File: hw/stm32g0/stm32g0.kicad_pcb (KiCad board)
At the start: 4 copper layers, 80 x 40 mm, 62 parts, among them J101 Barrel_Jack_Switch, J102 Screw_Terminal_01x03, J201 Conn_01x06, J202 Conn_01x04, J203 Conn_01x03, Q101 BC817, SW401 SW_Push, SW402 SW_Push, SW403 SW_Push, SW404 SW_Push, SW405 SW_Push, SW406 SW_Push, U201 STM32G030K8Tx, U202 74AHCT125, U203 CAT24C256, U301 VS1838B, U401 4050, U501 AMS1117-3.3

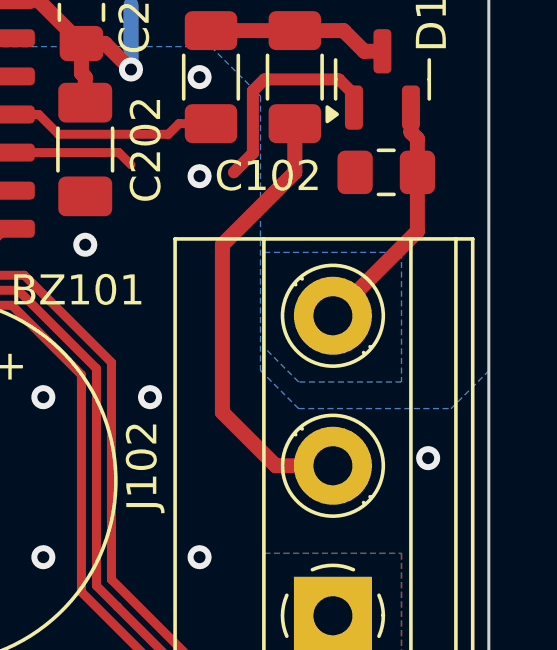
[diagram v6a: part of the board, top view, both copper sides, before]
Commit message: chore(hw): add cable connector identifiers
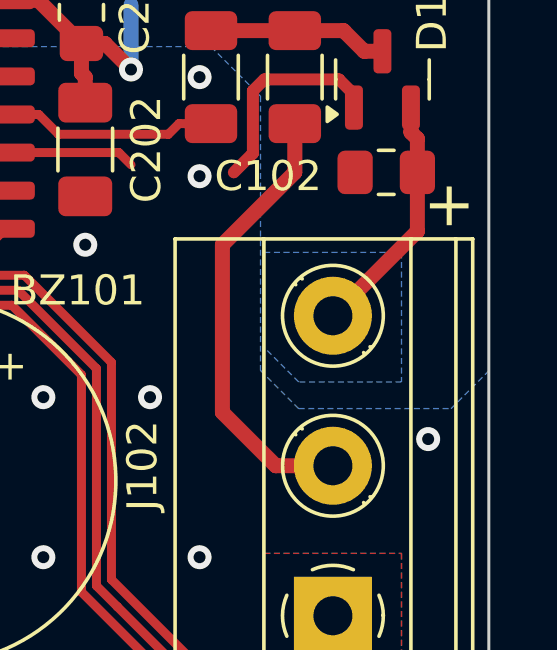
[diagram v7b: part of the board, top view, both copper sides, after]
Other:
- board text added: "+"
- board text added: "-"
- board text added: "D"
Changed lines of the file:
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@@
 		)
 	)
+	(gr_text "D"
+		(at 196.342 93.853 -90)
+		(layer "B.SilkS")
+		(effects
+			(font
+				(size 1.5 1.5)
+				(thickness 0.15)
+			)
+			(justify left bottom)
+		)
+	)
+	(gr_text "-"
+		(at 196.342 98.679 -90)
+		(layer "B.SilkS")
+		(effects
+			(font
+				(size 1.5 1.5)
+				(thickness 0.15)
+			)
+			(justify left bottom)
+		)
+	)
 	(gr_text "JLCJLCJLCJLC"
 		(at 186.563 76.835 0)
@@
 		)
 	)
+	(gr_text "+"
+		(at 196.342 88.646 -90)
+		(layer "B.SilkS")
+		(effects
+			(font
+				(size 1.5 1.5)
+				(thickness 0.15)
+			)
+			(justify left bottom)
+		)
+	)
 	(gr_text "R"
 		(at 174.752 81.788 0)
@@
 		)
 	)
+	(gr_text "+"
+		(at 197.231 85.09 270)
+		(layer "F.SilkS")
+		(effects
+			(font
+				(size 1.5 1.5)
+				(thickness 0.15)
+			)
+			(justify left bottom)
+		)
+	)
 	(gr_text "G"
 		(at 174.752 86.36 0)
@@
 	)
 	(via
-		(at 197.358 94.361)
+		(at 197.358 93.726)
 		(size 0.8)
 		(drill 0.4)
@@
 	)
 	(group ""
+		(members "ac98b90d-8acc-4557-9752-f28e7031f9e1" "acbd161f-f8ce-4742-a507-e40d7ef71db5"
+			"f7fb9be6-987a-44a3-bb12-16e19cd526a0"
+		)
+	)
+	(group ""

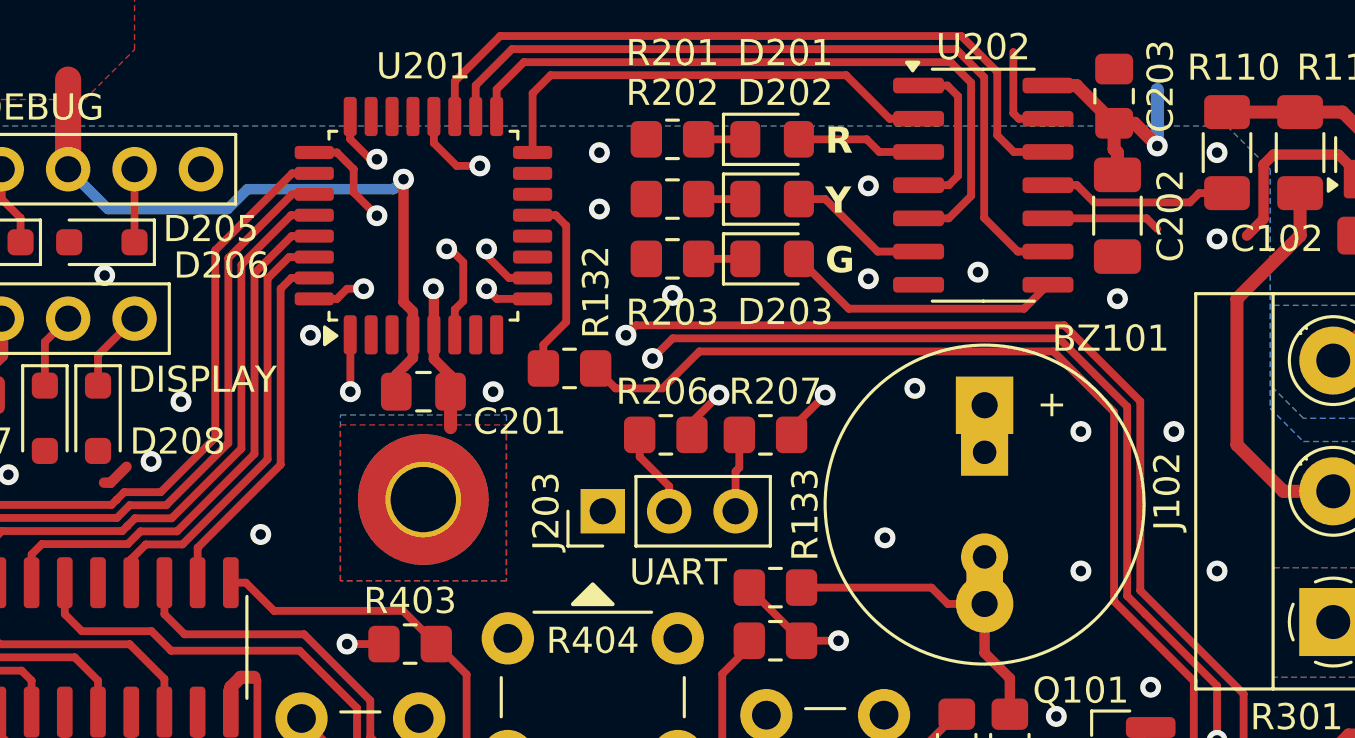
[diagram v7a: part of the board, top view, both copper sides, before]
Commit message: chore(hw): increase CPU decoupling
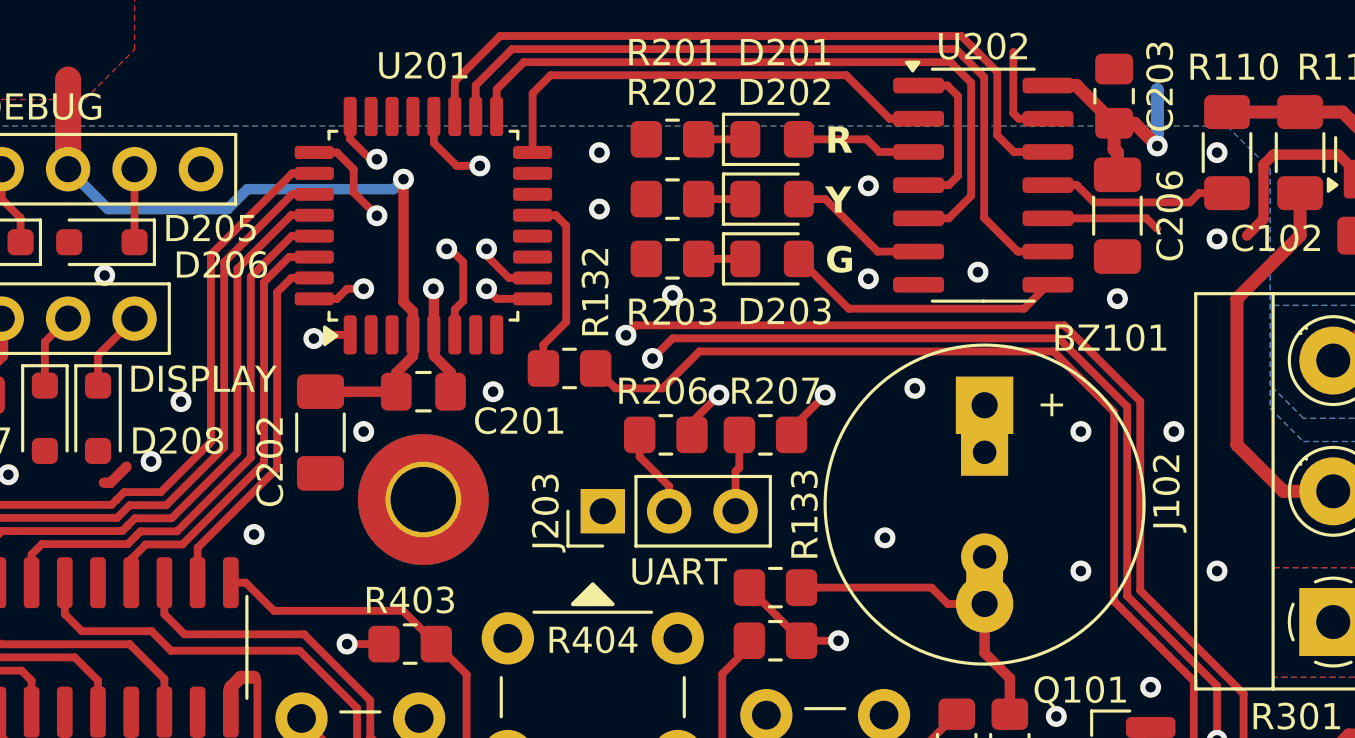
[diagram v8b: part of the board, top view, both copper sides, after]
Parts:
- added C206: 10u, Capacitor_SMD:C_1206_3216Metric_Pad1.33x1.80mm_HandSolder, F.Cu at (185.9, 84.1)
- moved C202 31.6 mm to (155.4, 92.4)
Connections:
- C202 pad 1: +5V -> +3.3V
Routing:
- net GND: track 277.5 -> 270.1 mm
- net +3.3V: track 187.8 -> 190.7 mm
- net /CPU/I2C_SDA: track 57.9 -> 59.4 mm
- net /CPU/I2C_SCL: track 60.1 -> 61.3 mm
